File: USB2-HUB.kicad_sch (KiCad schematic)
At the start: 31 parts, among them J11 USB_OTG, J13 690-008-221-904, U13 FSUSB42MUX, U4 TPD4EUSB30, U6 USB2514B-I/M2, U7 AP22653W6, Y1 24MHz

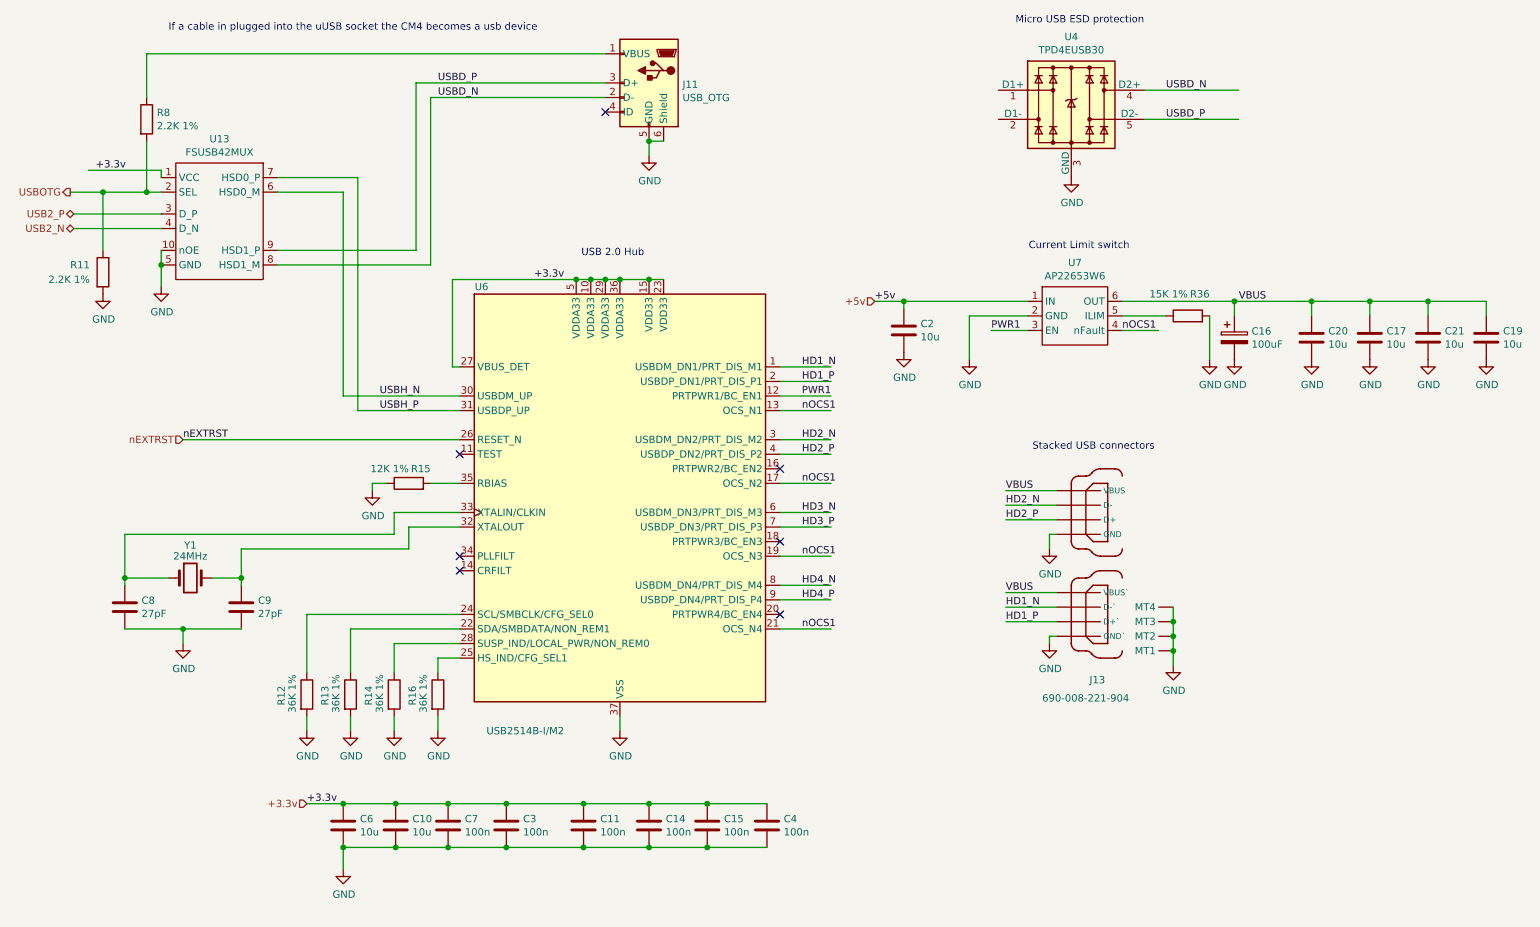
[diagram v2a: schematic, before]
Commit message: added the PSU control connector.
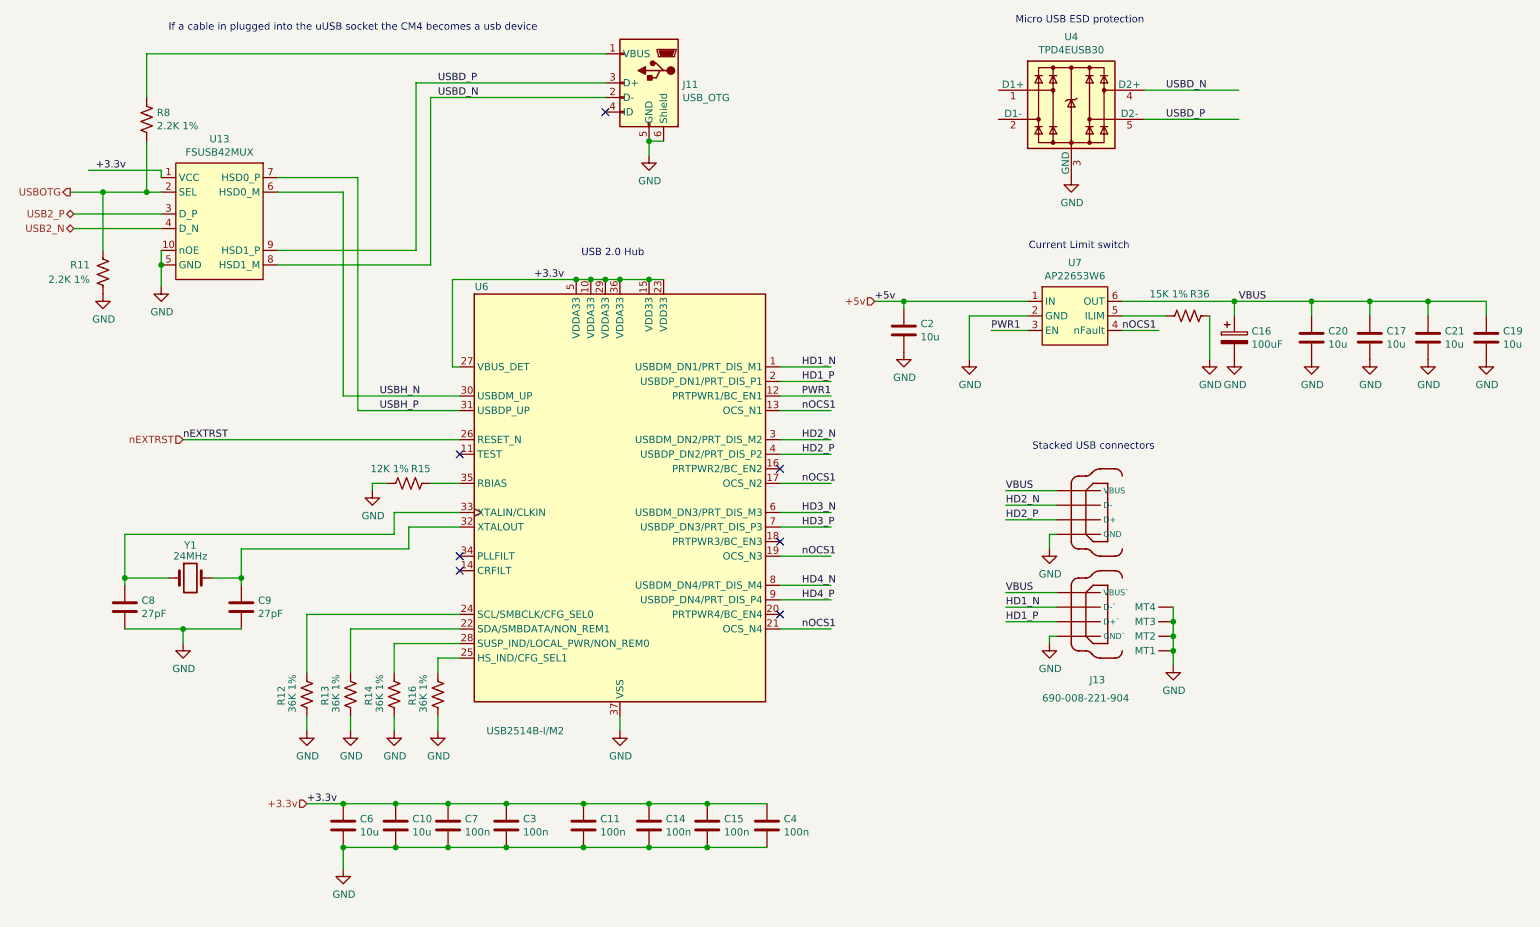
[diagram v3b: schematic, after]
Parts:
- R11, R12, R13, R14, R15, R16, R36, R8: symbol Device:R -> Device:R_US
- U7: Field5 31-AP22653W6-7CT-ND -> AP2553W6-7DICT-ND
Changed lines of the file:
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@@
     )
   )
-  (symbol (lib_id "Device:R") (at 40.64 45.72 0) (unit 1)
+  (symbol (lib_id "Device:R_US") (at 40.64 45.72 0) (unit 1)
     (in_bom yes) (on_board yes) (dnp no)
     (property "Reference" "R8" (at 42.418 44.5516 0)
@@
       (effects (font (size 1.27 1.27)) (justify left))
     )
-    (property "Footprint" "Resistor_SMD:R_0402_1005Metric" (at 38.862 45.72 90)
-      (effects (font (size 1.27 1.27)) hide)
-    )
-    (property "Datasheet" "https://fscdn.rohm.com/en/products/databook/datasheet/passive/resistor/chip_resistor/mcr-e.pdf" (at 40.64 45.72 0)
+    (property "Footprint" "Resistor_SMD:R_0402_1005Metric" (at 41.656 45.974 90)
+      (effects (font (size 1.27 1.27)) hide)
+    )
+    (property "Datasheet" "~" (at 40.64 45.72 0)
       (effects (font (size 1.27 1.27)) hide)
     )
@@
     )
   )
-  (symbol (lib_id "Device:R") (at 33.02 72.39 0) (unit 1)
+  (symbol (lib_id "Device:R_US") (at 33.02 72.39 0) (unit 1)
     (in_bom yes) (on_board yes) (dnp no)
     (property "Reference" "R11" (at 27.305 71.12 0)
@@
       (effects (font (size 1.27 1.27)) (justify left))
     )
-    (property "Footprint" "Resistor_SMD:R_0402_1005Metric" (at 31.242 72.39 90)
-      (effects (font (size 1.27 1.27)) hide)
-    )
-    (property "Datasheet" "https://fscdn.rohm.com/en/products/databook/datasheet/passive/resistor/chip_resistor/mcr-e.pdf" (at 33.02 72.39 0)
+    (property "Footprint" "Resistor_SMD:R_0402_1005Metric" (at 34.036 72.644 90)
+      (effects (font (size 1.27 1.27)) hide)
+    )
+    (property "Datasheet" "~" (at 33.02 72.39 0)
       (effects (font (size 1.27 1.27)) hide)
     )
@@
       (effects (font (size 1.27 1.27)) hide)
     )
-    (property "Field5" "	31-AP22653W6-7CT-ND" (at 203.2 80.01 0)
+    (property "Field5" "AP2553W6-7DICT-ND" (at 203.2 80.01 0)
       (effects (font (size 1.27 1.27)) hide)
     )
@@
     )
   )
-  (symbol (lib_id "Device:R") (at 83.82 146.05 0) (unit 1)
+  (symbol (lib_id "Device:R_US") (at 83.82 146.05 0) (unit 1)
     (in_bom yes) (on_board yes) (dnp no)
     (property "Reference" "R14" (at 79.375 147.955 90)
@@
       (effects (font (size 1.27 1.27)) (justify left))
     )
-    (property "Footprint" "Resistor_SMD:R_0402_1005Metric" (at 82.042 146.05 90)
-      (effects (font (size 1.27 1.27)) hide)
-    )
-    (property "Datasheet" "https://fscdn.rohm.com/en/products/databook/datasheet/passive/resistor/chip_resistor/mcr-e.pdf" (at 83.82 146.05 0)
+    (property "Footprint" "Resistor_SMD:R_0402_1005Metric" (at 84.836 146.304 90)
+      (effects (font (size 1.27 1.27)) hide)
+    )
+    (property "Datasheet" "~" (at 83.82 146.05 0)
       (effects (font (size 1.27 1.27)) hide)
     )
@@
     )
   )
-  (symbol (lib_id "Device:R") (at 76.2 146.05 0) (unit 1)
+  (symbol (lib_id "Device:R_US") (at 76.2 146.05 0) (unit 1)
     (in_bom yes) (on_board yes) (dnp no)
     (property "Reference" "R13" (at 71.755 147.955 90)
@@
       (effects (font (size 1.27 1.27)) (justify left))
     )
-    (property "Footprint" "Resistor_SMD:R_0402_1005Metric" (at 74.422 146.05 90)
-      (effects (font (size 1.27 1.27)) hide)
-    )
-    (property "Datasheet" "https://fscdn.rohm.com/en/products/databook/datasheet/passive/resistor/chip_resistor/mcr-e.pdf" (at 76.2 146.05 0)
+    (property "Footprint" "Resistor_SMD:R_0402_1005Metric" (at 77.216 146.304 90)
+      (effects (font (size 1.27 1.27)) hide)
+    )
+    (property "Datasheet" "~" (at 76.2 146.05 0)
       (effects (font (size 1.27 1.27)) hide)
     )
@@
     )
   )
-  (symbol (lib_id "Device:R") (at 68.58 146.05 0) (unit 1)
+  (symbol (lib_id "Device:R_US") (at 68.58 146.05 0) (unit 1)
     (in_bom yes) (on_board yes) (dnp no)
     (property "Reference" "R12" (at 64.135 147.955 90)
@@
       (effects (font (size 1.27 1.27)) (justify left))
     )
-    (property "Footprint" "Resistor_SMD:R_0402_1005Metric" (at 66.802 146.05 90)
-      (effects (font (size 1.27 1.27)) hide)
-    )
-    (property "Datasheet" "https://fscdn.rohm.com/en/products/databook/datasheet/passive/resistor/chip_resistor/mcr-e.pdf" (at 68.58 146.05 0)
+    (property "Footprint" "Resistor_SMD:R_0402_1005Metric" (at 69.596 146.304 90)
+      (effects (font (size 1.27 1.27)) hide)
+    )
+    (property "Datasheet" "~" (at 68.58 146.05 0)
       (effects (font (size 1.27 1.27)) hide)
     )
@@
     )
   )
-  (symbol (lib_id "Device:R") (at 222.25 80.01 90) (unit 1)
+  (symbol (lib_id "Device:R_US") (at 222.25 80.01 90) (unit 1)
     (in_bom yes) (on_board yes) (dnp no)
     (property "Reference" "R36" (at 226.06 76.2 90)
@@
       (effects (font (size 1.27 1.27)) (justify left))
     )
-    (property "Footprint" "Resistor_SMD:R_0402_1005Metric" (at 222.25 81.788 90)
-      (effects (font (size 1.27 1.27)) hide)
-    )
-    (property "Datasheet" "https://fscdn.rohm.com/en/products/databook/datasheet/passive/resistor/chip_resistor/mcr-e.pdf" (at 222.25 80.01 0)
+    (property "Footprint" "Resistor_SMD:R_0402_1005Metric" (at 222.504 78.994 90)
+      (effects (font (size 1.27 1.27)) hide)
+    )
+    (property "Datasheet" "~" (at 222.25 80.01 0)
       (effects (font (size 1.27 1.27)) hide)
     )
@@
     )
   )
-  (symbol (lib_id "Device:R") (at 86.36 109.22 90) (unit 1)
+  (symbol (lib_id "Device:R_US") (at 86.36 109.22 90) (unit 1)
     (in_bom yes) (on_board yes) (dnp no)
     (property "Reference" "R15" (at 90.17 106.68 90)
@@
       (effects (font (size 1.27 1.27)) (justify left))
     )
-    (property "Footprint" "Resistor_SMD:R_0402_1005Metric" (at 86.36 110.998 90)
-      (effects (font (size 1.27 1.27)) hide)
-    )
-    (property "Datasheet" "https://fscdn.rohm.com/en/products/databook/datasheet/passive/resistor/chip_resistor/mcr-e.pdf" (at 86.36 109.22 0)
+    (property "Footprint" "Resistor_SMD:R_0402_1005Metric" (at 86.614 108.204 90)
+      (effects (font (size 1.27 1.27)) hide)
+    )
+    (property "Datasheet" "~" (at 86.36 109.22 0)
       (effects (font (size 1.27 1.27)) hide)
     )
@@
     )
   )
-  (symbol (lib_id "Device:R") (at 91.44 146.05 0) (unit 1)
+  (symbol (lib_id "Device:R_US") (at 91.44 146.05 0) (unit 1)
     (in_bom yes) (on_board yes) (dnp no)
     (property "Reference" "R16" (at 86.995 147.955 90)
@@
       (effects (font (size 1.27 1.27)) (justify left))
     )
-    (property "Footprint" "Resistor_SMD:R_0402_1005Metric" (at 89.662 146.05 90)
-      (effects (font (size 1.27 1.27)) hide)
-    )
-    (property "Datasheet" "https://fscdn.rohm.com/en/products/databook/datasheet/passive/resistor/chip_resistor/mcr-e.pdf" (at 91.44 146.05 0)
-      (effects (font (size 1.27 1.27)) hide)
-    )
+    (property "Footprint" "Resistor_SMD:R_0402_1005Metric" (at 92.456 146.304 90)
+      (effects (font (size 1.27 1.27)) hide)
+    )
+    (property "Datasheet" "~" (at 91.44 146.05 0)
+      (effects (font (size 1.27 1.27)) hide)
+    )

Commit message: finding/adding digikey part numbers
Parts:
- J11: DK (none) -> 609-4050-2-ND; Field4 Digikey -> (none); Field5 609-4050-2-ND -> (none); Field6 690-005-298-486 -> (none); Field7 EDAC -> (none); Field8 UCON00686 -> (none); PARTNO (none) -> 10103594-0001LF; Part Description USB - micro B USB 2.0 Receptacle Connector 5 Position Surfa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 -> (none)
- J13: DK (none) -> WM17130-ND; Field4 Farnell -> (none); Field5 2751688 -> (none); Field6 690-008-221-904 -> (none); Field7 EDAC -> (none); Field8 UCON00727 -> (none); PARTNO (none) -> 0672984090; Part Description USB-A (USB TYPE-A), Stacked Receptacle Connector 8 Position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 -> (none)
- U13: DK (none) -> FSUSB42MUXCT-ND; Field4 Farnell -> (none); Field5 2564479 -> (none); Field6 FSUSB42MUX -> (none); Field7 Onsemi -> (none); PARTNO (none) -> FSUSB42MUX; Part Description USB Switch IC 1 Channel 10-MSOP -> (none)
- U4: DK (none) -> 296-28063-1-ND; Field4 Farnell -> (none); Field5 2335455 -> (none); Field6 CDDFN10-3324P-13 -> (none); Field7 Bourns -> (none); Field8 UDIO00346 -> (none); PARTNO (none) -> TPD4EUSB30DQAR; Part Description Quad TVS diode for high speed signals (USB3, GigE etc.) -> (none)
- U6: DK (none) -> USB2514B-I/M2-ND; Field4 Farnell -> (none); Field5 2775060 -> (none); Field6 USB2514B-I/M2 -> (none); Field7 Microchip -> (none); Field8 UICC00931 -> (none); PARTNO (none) -> USB2514B-I/M2; Part Description USB Hub Controller USB Interface 36-SQFN (6x6) -> (none)
- U7: DK (none) -> AP2553W6-7DICT-ND; Field4 Digikey -> (none); Field5 AP2553W6-7DICT-ND -> (none); Field6 AP22653W6 -> (none); Field7 Diodes -> (none); PARTNO (none) -> AP2553W6-7; Part Description Power Switch/Driver 1:1 P-Channel 2.1A SOT-23-6 -> (none)
- Y1: footprint Crystal:Crystal_SMD_HC49-SD -> bitcart:CRYSTAL_ABM8G_ABR; symbol Device:Crystal -> Device:Crystal_13; DK (none) -> 535-10273-1-ND; Field4 Farnell -> (none); Field5 2508493 -> (none); Field6 X24M000000S128 -> (none); Field7 AEL -> (none); PARTNO (none) -> ABM8G-24.000MHZ-18-D2Y-T; Part Description 24MHz Crystal 18pf 30ppm 30ppm -> (none)
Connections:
- net at C9.1, U6.32 (XTALOUT): now also Y1.3; no longer Y1.2
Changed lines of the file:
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@@
       (effects (font (size 1.27 1.27)) (justify left bottom) hide)
     )
-    (property "Field4" "Farnell" (at 207.01 125.73 0)
-      (effects (font (size 1.27 1.27)) (justify left bottom) hide)
-    )
-    (property "Field5" "	2751688" (at 207.01 125.73 0)
-      (effects (font (size 1.27 1.27)) (justify left bottom) hide)
-    )
-    (property "Field6" "690-008-221-904" (at 207.01 125.73 0)
-      (effects (font (size 1.27 1.27)) (justify left bottom) hide)
-    )
-    (property "Field7" "EDAC" (at 207.01 125.73 0)
-      (effects (font (size 1.27 1.27)) (justify left bottom) hide)
-    )
-    (property "Field8" "UCON00727" (at 207.01 125.73 0)
-      (effects (font (size 1.27 1.27)) (justify left bottom) hide)
-    )
-    (property "Part Description" "USB-A (USB TYPE-A), Stacked Receptacle Connector 8 Position Through Hole, Right Angle" (at 207.01 125.73 0)
+    (property "DK" "WM17130-ND" (at 207.01 125.73 0)
+      (effects (font (size 1.27 1.27)) hide)
+    )
+    (property "PARTNO" "0672984090" (at 207.01 125.73 0)
       (effects (font (size 1.27 1.27)) hide)
     )
@@
       (effects (font (size 1.27 1.27)) hide)
     )
-    (property "Field4" "Digikey" (at 128.27 39.37 0)
-      (effects (font (size 1.27 1.27)) hide)
-    )
-    (property "Field5" "609-4050-2-ND" (at 128.27 39.37 0)
-      (effects (font (size 1.27 1.27)) hide)
-    )
-    (property "Field6" "690-005-298-486" (at 128.27 39.37 0)
-      (effects (font (size 1.27 1.27)) hide)
-    )
-    (property "Field7" "EDAC" (at 128.27 39.37 0)
-      (effects (font (size 1.27 1.27)) hide)
-    )
-    (property "Part Description" "USB - micro B USB 2.0 Receptacle Connector 5 Position Surface Mount, Right Angle; Through Hole" (at 128.27 39.37 0)
-      (effects (font (size 1.27 1.27)) hide)
-    )
-    (property "Field8" "UCON00686" (at 128.27 39.37 0)
+    (property "PARTNO" "10103594-0001LF" (at 128.27 39.37 0)
+      (effects (font (size 1.27 1.27)) hide)
+    )
+    (property "DK" "609-4050-2-ND" (at 128.27 39.37 0)
       (effects (font (size 1.27 1.27)) hide)
     )
@@
       (effects (font (size 1.27 1.27)) hide)
     )
-    (property "Field4" "Digikey" (at 203.2 80.01 0)
-      (effects (font (size 1.27 1.27)) hide)
-    )
-    (property "Field5" "AP2553W6-7DICT-ND" (at 203.2 80.01 0)
-      (effects (font (size 1.27 1.27)) hide)
-    )
-    (property "Field6" "AP22653W6" (at 203.2 80.01 0)
-      (effects (font (size 1.27 1.27)) hide)
-    )
-    (property "Field7" "Diodes" (at 203.2 80.01 0)
-      (effects (font (size 1.27 1.27)) hide)
-    )
-    (property "Part Description" "	Power Switch/Driver 1:1 P-Channel 2.1A SOT-23-6" (at 203.2 80.01 0)
+    (property "DK" "AP2553W6-7DICT-ND" (at 203.2 80.01 0)
+      (effects (font (size 1.27 1.27)) hide)
+    )
+    (property "PARTNO" "AP2553W6-7" (at 203.2 80.01 0)
       (effects (font (size 1.27 1.27)) hide)
     )
@@
       (effects (font (size 1.27 1.27)) hide)
     )
-    (property "Field4" "Farnell" (at 123.19 111.76 0)
-      (effects (font (size 1.27 1.27)) hide)
-    )
-    (property "Field5" "2775060" (at 123.19 111.76 0)
-      (effects (font (size 1.27 1.27)) hide)
-    )
-    (property "Field6" "USB2514B-I/M2" (at 123.19 111.76 0)
-      (effects (font (size 1.27 1.27)) hide)
-    )
-    (property "Field7" "Microchip" (at 123.19 111.76 0)
-      (effects (font (size 1.27 1.27)) hide)
-    )
-    (property "Part Description" "	USB Hub Controller USB Interface 36-SQFN (6x6)" (at 123.19 111.76 0)
-      (effects (font (size 1.27 1.27)) hide)
-    )
-    (property "Field8" "UICC00931" (at 123.19 111.76 0)
+    (property "DK" "USB2514B-I/M2-ND" (at 123.19 111.76 0)
+      (effects (font (size 1.27 1.27)) hide)
+    )
+    (property "PARTNO" "USB2514B-I/M2" (at 123.19 111.76 0)
       (effects (font (size 1.27 1.27)) hide)
     )
@@
       (effects (font (size 1.27 1.27)) hide)
     )
-    (property "Field4" "Farnell" (at 52.07 72.39 0)
-      (effects (font (size 1.27 1.27)) hide)
-    )
-    (property "Field5" "2564479" (at 52.07 72.39 0)
-      (effects (font (size 1.27 1.27)) hide)
-    )
-    (property "Field6" "FSUSB42MUX" (at 52.07 72.39 0)
-      (effects (font (size 1.27 1.27)) hide)
-    )
-    (property "Field7" "Onsemi" (at 52.07 72.39 0)
-      (effects (font (size 1.27 1.27)) hide)
-    )
-    (property "Part Description" "USB Switch IC 1 Channel 10-MSOP" (at 52.07 72.39 0)
+    (property "DK" "FSUSB42MUXCT-ND" (at 52.07 72.39 0)
+      (effects (font (size 1.27 1.27)) hide)
+    )
+    (property "PARTNO" "FSUSB42MUX" (at 52.07 72.39 0)
       (effects (font (size 1.27 1.27)) hide)
     )
@@
     )
   )
-  (symbol (lib_id "Device:Crystal") (at 48.26 125.73 0) (unit 1)
+  (symbol (lib_id "Device:Crystal_13") (at 48.26 125.73 0) (unit 1)
     (in_bom yes) (on_board yes) (dnp no)
     (property "Reference" "Y1" (at 48.26 120.015 0)
@@
       (effects (font (size 1.27 1.27)))
     )
-    (property "Footprint" "Crystal:Crystal_SMD_HC49-SD" (at 48.26 125.73 0)
-      (effects (font (size 1.27 1.27)) hide)
-    )
-    (property "Datasheet" "~" (at 48.26 125.73 0)
-      (effects (font (size 1.27 1.27)) hide)
-    )
-    (property "Field4" "Farnell" (at 48.26 125.73 0)
-      (effects (font (size 1.27 1.27)) hide)
-    )
-    (property "Field5" "2508493" (at 48.26 125.73 0)
-      (effects (font (size 1.27 1.27)) hide)
-    )
-    (property "Field7" "AEL" (at 48.26 125.73 0)
-      (effects (font (size 1.27 1.27)) hide)
-    )
-    (property "Field6" "X24M000000S128" (at 48.26 125.73 0)
-      (effects (font (size 1.27 1.27)) hide)
-    )
-    (property "Part Description" "24MHz Crystal 18pf 30ppm 30ppm" (at 48.26 125.73 0)
-      (effects (font (size 1.27 1.27)) hide)
-    )
-    (pin "1")
-    (pin "2")
+    (property "Footprint" "bitcart:CRYSTAL_ABM8G_ABR" (at 48.26 125.73 0)
+      (effects (font (size 1.27 1.27)) hide)
+    )
+    (property "Datasheet" "https://abracon.com/Resonators/ABM8G.pdf" (at 48.26 125.73 0)
+      (effects (font (size 1.27 1.27)) hide)
+    )
+    (property "DK" "535-10273-1-ND" (at 48.26 125.73 0)
+      (effects (font (size 1.27 1.27)) hide)
+    )
+    (property "PARTNO" "ABM8G-24.000MHZ-18-D2Y-T" (at 48.26 125.73 0)
+      (effects (font (size 1.27 1.27)) hide)
+    )
+    (pin "1")
+    (pin "3")
     (instances
       (project "bitcart"
@@
       (effects (font (size 1.27 1.27)) hide)
     )
-    (property "Field4" "Farnell" (at 201.93 43.18 0)
-      (effects (font (size 1.27 1.27)) hide)
-    )
-    (property "Field5" "2335455" (at 201.93 43.18 0)
-      (effects (font (size 1.27 1.27)) hide)
-    )
-    (property "Field6" "CDDFN10-3324P-13" (at 201.93 43.18 0)
-      (effects (font (size 1.27 1.27)) hide)
-    )
-    (property "Field7" "Bourns" (at 201.93 43.18 0)
-      (effects (font (size 1.27 1.27)) hide)
-    )
-    (property "Field8" "UDIO00346" (at 201.93 43.18 0)
-      (effects (font (size 1.27 1.27)) hide)
-    )
-    (property "Part Description" "Quad TVS diode for high speed signals (USB3, GigE etc.)" (at 201.93 43.18 0)
-      (effects (font (size 1.27 1.27)) hide)
-    )
+    (property "DK" "296-28063-1-ND" (at 201.93 43.18 0)
+      (effects (font (size 1.27 1.27)) hide)
+    )
+    (property "PARTNO" "TPD4EUSB30DQAR" (at 201.93 43.18 0)
+      (effects (font (size 1.27 1.27)) hide)
+    )
